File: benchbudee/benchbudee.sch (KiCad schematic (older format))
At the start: 0 parts

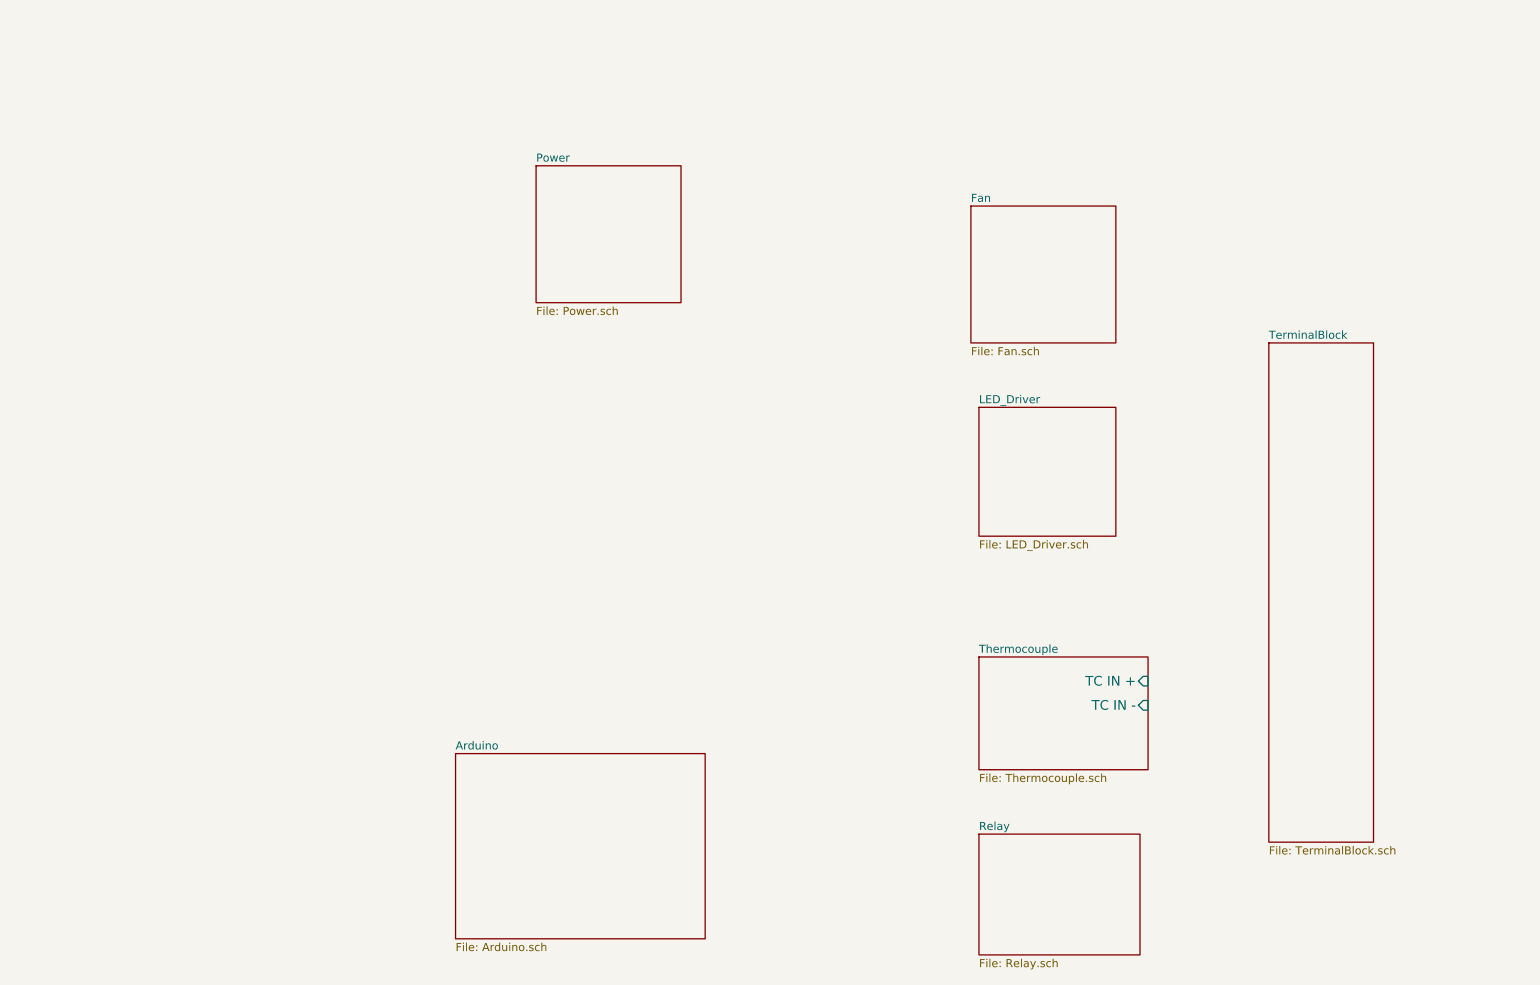
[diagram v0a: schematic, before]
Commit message: Added signals
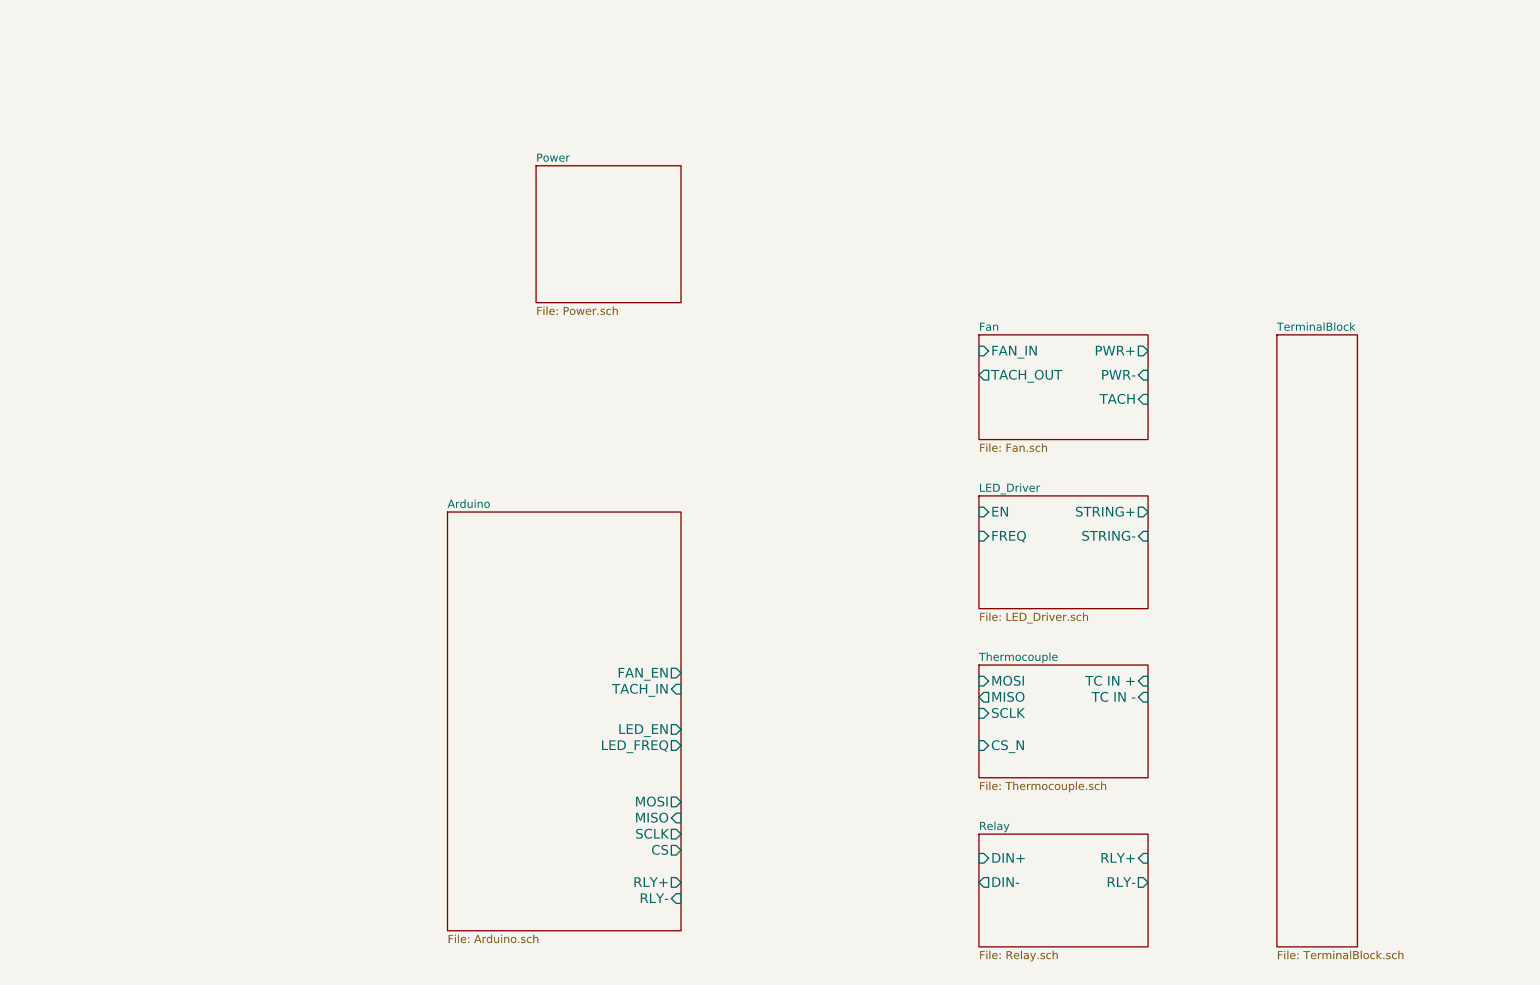
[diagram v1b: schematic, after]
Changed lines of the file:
@@
 $EndDescr
 $Sheet
-S 3850 5450 1550 1150
+S 3800 3950 1450 2600
 U 52F13E2E
 F0 "Arduino" 50
 F1 "Arduino.sch" 50
+F2 "RLY+" O R 5250 6250 60
+F3 "RLY-" I R 5250 6350 60
+F4 "MOSI" O R 5250 5750 60
+F5 "MISO" I R 5250 5850 60
+F6 "SCLK" O R 5250 5950 60
+F7 "CS" O R 5250 6050 60
+F8 "LED_EN" O R 5250 5300 60
+F9 "LED_FREQ" O R 5250 5400 60
+F10 "FAN_EN" O R 5250 4950 60
+F11 "TACH_IN" I R 5250 5050 60
 $EndSheet
 $Sheet
-S 7100 4850 1050 700
+S 7100 4900 1050 700
 U 52F13E8B
 F0 "Thermocouple" 50
 F1 "Thermocouple.sch" 50
 F2 "TC IN +" I R 8150 5000 60
-F3 "TC IN -" I R 8150 5150 60
+F3 "TC IN -" I R 8150 5100 60
+F4 "MOSI" I L 7100 5000 60
+F5 "MISO" O L 7100 5100 60
+F6 "SCLK" I L 7100 5200 60
+F7 "CS_N" I L 7100 5400 60
 $EndSheet
 $Sheet
-S 7100 5950 1000 750
+S 7100 5950 1050 700
 U 52F13E9E
 F0 "Relay" 50
 F1 "Relay.sch" 50
+F2 "RLY+" I R 8150 6100 60
+F3 "RLY-" O R 8150 6250 60
+F4 "DIN+" I L 7100 6100 60
+F5 "DIN-" O L 7100 6250 60
 $EndSheet
 $Sheet
@@
 $EndSheet
 $Sheet
-S 7100 3300 850  800
+S 7100 3850 1050 700
 U 52F1408A
 F0 "LED_Driver" 50
 F1 "LED_Driver.sch" 50
+F2 "EN" I L 7100 3950 60
+F3 "FREQ" I L 7100 4100 60
+F4 "STRING+" O R 8150 3950 60
+F5 "STRING-" I R 8150 4100 60
 $EndSheet
 $Sheet
-S 7050 2050 900  850
+S 7100 2850 1050 650
 U 52F140AA
 F0 "Fan" 50
 F1 "Fan.sch" 50
+F2 "PWR+" O R 8150 2950 60
+F3 "PWR-" I R 8150 3100 60
+F4 "TACH" I R 8150 3250 60
+F5 "TACH_OUT" O L 7100 3100 60
+F6 "FAN_IN" I L 7100 2950 60
 $EndSheet
 $Sheet
-S 8900 2900 650  3100
+S 8950 2850 500  3800
 U 52F140D2
 F0 "TerminalBlock" 50

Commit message: Added block diagram and thermocouple schematic
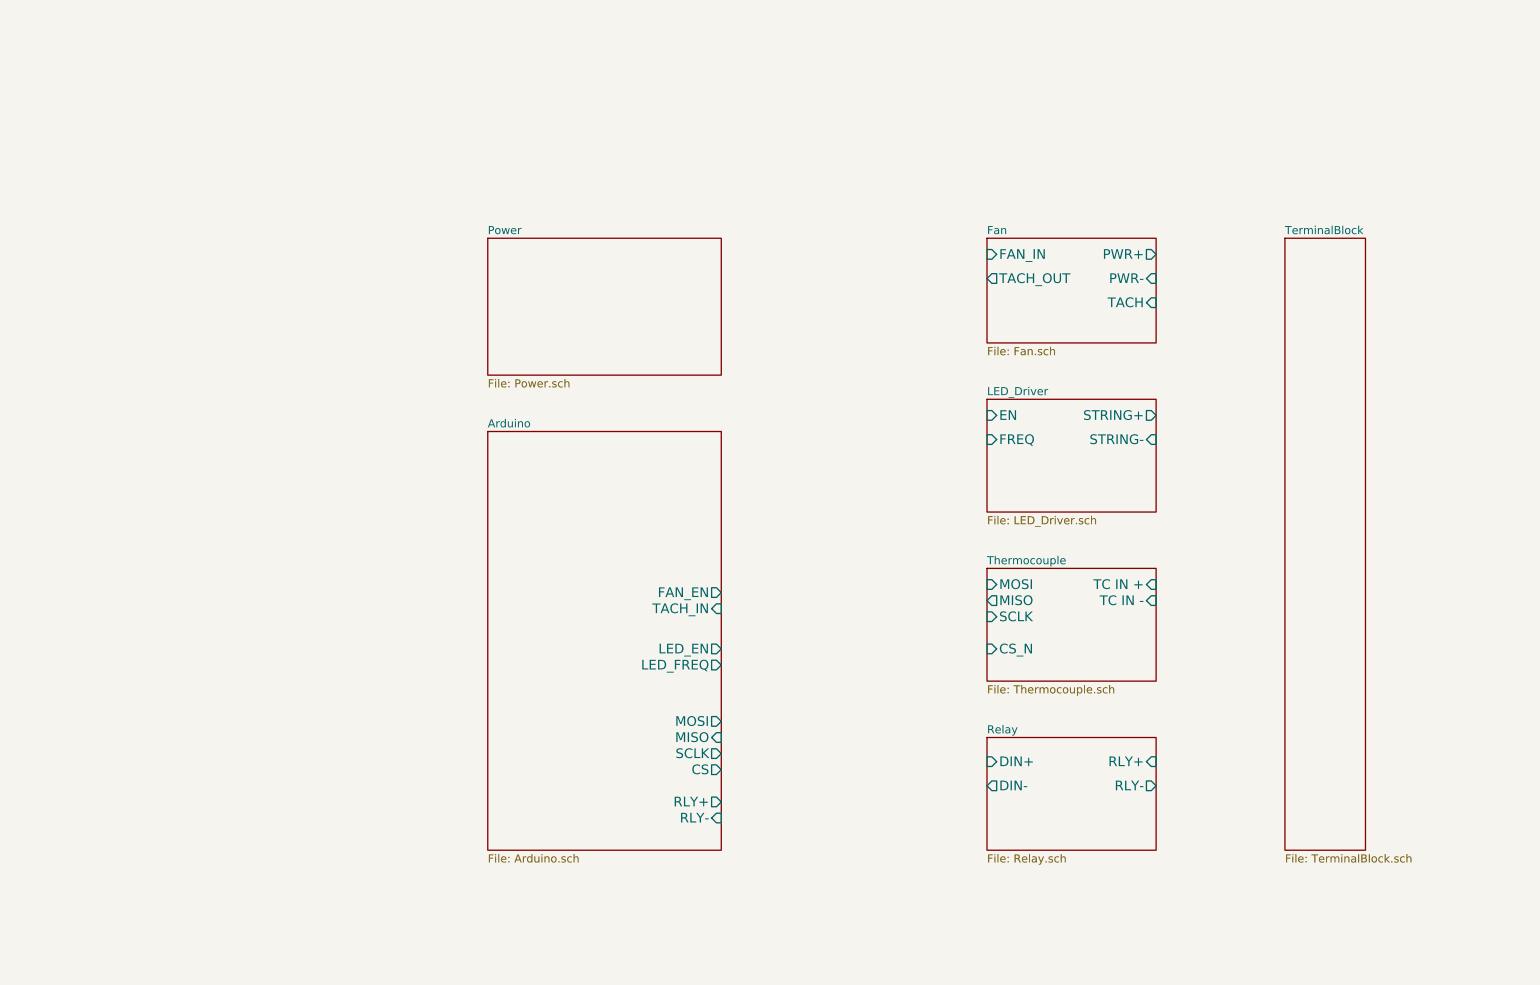
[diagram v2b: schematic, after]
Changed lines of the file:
@@
 Sheet 1 8
 Title ""
-Date "4 feb 2014"
+Date "12 feb 2014"
 Rev ""
 Comp ""
@@
 $EndDescr
 $Sheet
-S 3800 3950 1450 2600
+S 4050 3450 1450 2600
 U 52F13E2E
 F0 "Arduino" 50
 F1 "Arduino.sch" 50
-F2 "RLY+" O R 5250 6250 60
-F3 "RLY-" I R 5250 6350 60
-F4 "MOSI" O R 5250 5750 60
-F5 "MISO" I R 5250 5850 60
-F6 "SCLK" O R 5250 5950 60
-F7 "CS" O R 5250 6050 60
-F8 "LED_EN" O R 5250 5300 60
-F9 "LED_FREQ" O R 5250 5400 60
-F10 "FAN_EN" O R 5250 4950 60
-F11 "TACH_IN" I R 5250 5050 60
+F2 "RLY+" O R 5500 5750 60
+F3 "RLY-" I R 5500 5850 60
+F4 "MOSI" O R 5500 5250 60
+F5 "MISO" I R 5500 5350 60
+F6 "SCLK" O R 5500 5450 60
+F7 "CS" O R 5500 5550 60
+F8 "LED_EN" O R 5500 4800 60
+F9 "LED_FREQ" O R 5500 4900 60
+F10 "FAN_EN" O R 5500 4450 60
+F11 "TACH_IN" I R 5500 4550 60
 $EndSheet
 $Sheet
-S 7100 4900 1050 700
+S 7150 4300 1050 700
 U 52F13E8B
 F0 "Thermocouple" 50
 F1 "Thermocouple.sch" 50
-F2 "TC IN +" I R 8150 5000 60
-F3 "TC IN -" I R 8150 5100 60
-F4 "MOSI" I L 7100 5000 60
-F5 "MISO" O L 7100 5100 60
-F6 "SCLK" I L 7100 5200 60
-F7 "CS_N" I L 7100 5400 60
+F2 "TC IN +" I R 8200 4400 60
+F3 "TC IN -" I R 8200 4500 60
+F4 "MOSI" I L 7150 4400 60
+F5 "MISO" O L 7150 4500 60
+F6 "SCLK" I L 7150 4600 60
+F7 "CS_N" I L 7150 4800 60
 $EndSheet
 $Sheet
-S 7100 5950 1050 700
+S 7150 5350 1050 700
 U 52F13E9E
 F0 "Relay" 50
 F1 "Relay.sch" 50
-F2 "RLY+" I R 8150 6100 60
-F3 "RLY-" O R 8150 6250 60
-F4 "DIN+" I L 7100 6100 60
-F5 "DIN-" O L 7100 6250 60
+F2 "RLY+" I R 8200 5500 60
+F3 "RLY-" O R 8200 5650 60
+F4 "DIN+" I L 7150 5500 60
+F5 "DIN-" O L 7150 5650 60
 $EndSheet
 $Sheet
-S 4350 1800 900  850
+S 4050 2250 1450 850
 U 52F1405E
 F0 "Power" 50
@@
 $EndSheet
 $Sheet
-S 7100 3850 1050 700
+S 7150 3250 1050 700
 U 52F1408A
 F0 "LED_Driver" 50
 F1 "LED_Driver.sch" 50
-F2 "EN" I L 7100 3950 60
-F3 "FREQ" I L 7100 4100 60
-F4 "STRING+" O R 8150 3950 60
-F5 "STRING-" I R 8150 4100 60
+F2 "EN" I L 7150 3350 60
+F3 "FREQ" I L 7150 3500 60
+F4 "STRING+" O R 8200 3350 60
+F5 "STRING-" I R 8200 3500 60
 $EndSheet
 $Sheet
-S 7100 2850 1050 650
+S 7150 2250 1050 650
 U 52F140AA
 F0 "Fan" 50
 F1 "Fan.sch" 50
-F2 "PWR+" O R 8150 2950 60
-F3 "PWR-" I R 8150 3100 60
-F4 "TACH" I R 8150 3250 60
-F5 "TACH_OUT" O L 7100 3100 60
-F6 "FAN_IN" I L 7100 2950 60
+F2 "PWR+" O R 8200 2350 60
+F3 "PWR-" I R 8200 2500 60
+F4 "TACH" I R 8200 2650 60
+F5 "TACH_OUT" O L 7150 2500 60
+F6 "FAN_IN" I L 7150 2350 60
 $EndSheet
 $Sheet
-S 8950 2850 500  3800
+S 9000 2250 500  3800
 U 52F140D2
 F0 "TerminalBlock" 50

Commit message: Added first crack at fan module
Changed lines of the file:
@@
-$EndSheet
-$Sheet
-S 7150 2250 1050 650
-U 52F140AA
-F0 "Fan" 50
-F1 "Fan.sch" 50
-F2 "PWR+" O R 8200 2350 60
-F3 "PWR-" I R 8200 2500 60
-F4 "TACH" I R 8200 2650 60
-F5 "TACH_OUT" O L 7150 2500 60
-F6 "FAN_IN" I L 7150 2350 60
 $EndSheet
 $Sheet
@@
 F1 "TerminalBlock.sch" 50
 $EndSheet
+$Sheet
+S 7150 1800 1050 1100
+U 52F140AA
+F0 "Fan" 50
+F1 "Fan.sch" 50
+F2 "PWR+" O R 8200 1900 60
+F3 "PWR-" I R 8200 2000 60
+F4 "TACH" I R 8200 2650 60
+F5 "TACH_OUT" O L 7150 2650 60
+F6 "FAN_IN" I L 7150 1900 60
+F7 "Current Measure" O L 7150 2800 60
+F8 "MOSI" I L 7150 2150 60
+F9 "MISO" O L 7150 2250 60
+F10 "CS_N" I L 7150 2350 60
+F11 "SCLK" I L 7150 2450 60
+$EndSheet
 $EndSCHEMATC

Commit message: Added first pass at the relay module.
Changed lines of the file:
@@
 LIBS:contrib
 LIBS:valves
+LIBS:benchbudee-custom
 LIBS:benchbudee-cache
 EELAYER 27 0
@@
 F0 "Relay" 50
 F1 "Relay.sch" 50
-F2 "RLY+" I R 8200 5500 60
-F3 "RLY-" O R 8200 5650 60
-F4 "DIN+" I L 7150 5500 60
-F5 "DIN-" O L 7150 5650 60
+F2 "DIN+" I L 7150 5500 60
+F3 "DIN-" O L 7150 5650 60
+F4 "NC" B R 8200 5500 60
+F5 "NO" B R 8200 5650 60
+F6 "COM" B R 8200 5800 60
 $EndSheet
 $Sheet

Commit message: Added Power Adjustment sheet.  Populated power sheet.
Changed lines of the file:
@@
 $Descr A4 11693 8268
 encoding utf-8
-Sheet 1 8
+Sheet 1 9
 Title ""
-Date "12 feb 2014"
+Date "13 feb 2014"
 Rev ""
 Comp ""
@@
 $EndDescr
 $Sheet
-S 4050 3450 1450 2600
+S 3050 3450 1450 2600
 U 52F13E2E
 F0 "Arduino" 50
 F1 "Arduino.sch" 50
-F2 "RLY+" O R 5500 5750 60
-F3 "RLY-" I R 5500 5850 60
-F4 "MOSI" O R 5500 5250 60
-F5 "MISO" I R 5500 5350 60
-F6 "SCLK" O R 5500 5450 60
-F7 "CS" O R 5500 5550 60
-F8 "LED_EN" O R 5500 4800 60
-F9 "LED_FREQ" O R 5500 4900 60
-F10 "FAN_EN" O R 5500 4450 60
-F11 "TACH_IN" I R 5500 4550 60
+F2 "RLY+" O R 4500 5750 60
+F3 "RLY-" I R 4500 5850 60
+F4 "MOSI" O R 4500 5250 60
+F5 "MISO" I R 4500 5350 60
+F6 "SCLK" O R 4500 5450 60
+F7 "CS" O R 4500 5550 60
+F8 "LED_EN" O R 4500 4800 60
+F9 "LED_FREQ" O R 4500 4900 60
+F10 "FAN_EN" O R 4500 4450 60
+F11 "TACH_IN" I R 4500 4550 60
 $EndSheet
 $Sheet
@@
 $EndSheet
 $Sheet
-S 4050 2250 1450 850
+S 1100 950  1450 850
 U 52F1405E
 F0 "Power" 50
@@
 $EndSheet
 $Sheet
-S 9000 2250 500  3800
+S 9400 1800 800  4250
 U 52F140D2
 F0 "TerminalBlock" 50
@@
 F11 "SCLK" I L 7150 2450 60
 $EndSheet
+$Sheet
+S 3600 950  1300 850
+U 52FC1BE1
+F0 "PowerAdjustmentMonitor" 50
+F1 "PowerAdjustmentMonitor.sch" 50
+$EndSheet
 $EndSCHEMATC
